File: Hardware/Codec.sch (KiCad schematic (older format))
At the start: 11 parts, among them U301 SGTL5000XNAA3

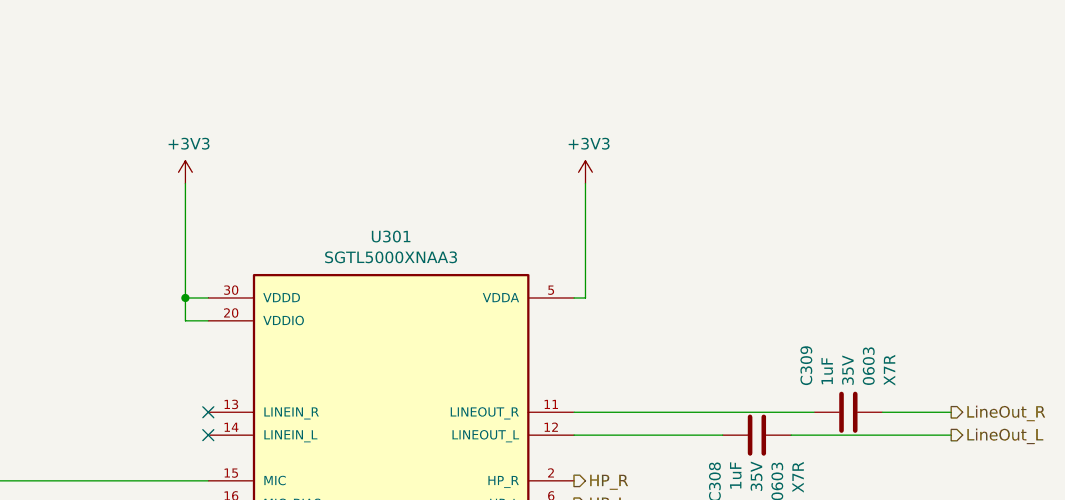
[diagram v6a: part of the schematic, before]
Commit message: Adding in extra decoupling.
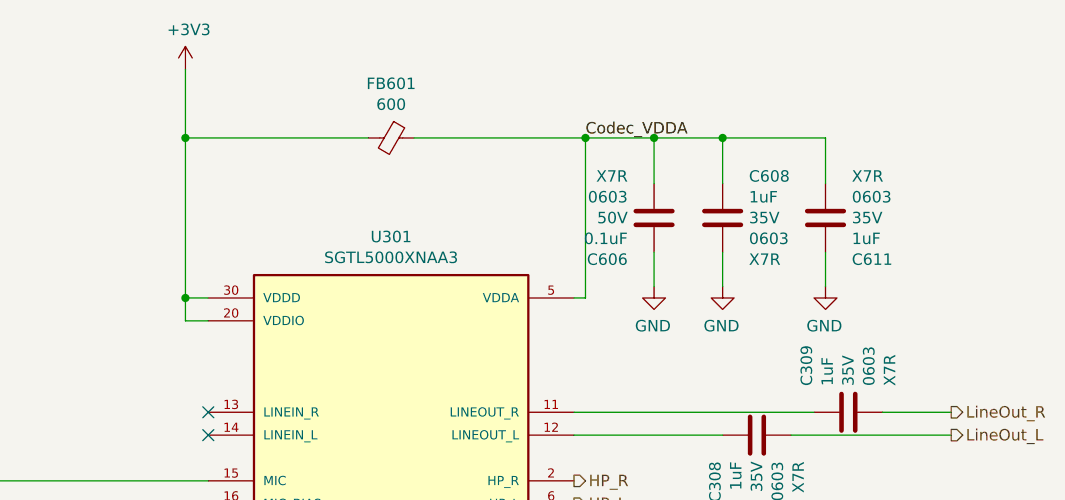
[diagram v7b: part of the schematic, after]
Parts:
- added C606: 0.1uF, Capacitor_SMD:C_0603_1608Metric, symbol Device:C
- added C608, C611: 1uF, Capacitor_SMD:C_0603_1608Metric, symbol Device:C
- added FB601: 600, Resistor_SMD:R_0603_1608Metric, symbol Device:Ferrite_Bead_Small
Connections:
- net +3V3: now also FB601.2; no longer U301.5 (VDDA)
- net GND: now also C606.1, C608.2, C611.1
- new net Codec_VDDA: C606.2, C608.1, C611.2, FB601.1, U301.5 (VDDA)
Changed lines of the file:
@@
 F 1 "SGTL5000XNAA3" H 5250 4726 50  0000 C CNN
 F 2 "Package_DFN_QFN:QFN-32-1EP_5x5mm_P0.5mm_EP3.65x3.65mm_ThermalVias" H 5250 3450 50  0001 L BNN
-F 3 "" H 5250 3450 50  0001 L BNN
+F 3 "https://www.nxp.com/docs/en/data-sheet/SGTL5000.pdf" H 5250 3450 50  0001 L BNN
 F 4 "Freescale Semiconductor" H 5250 3450 50  0001 L BNN "MANUFACTURER"
 F 5 "SGTL5000XNAA3" H 5250 3450 50  0001 C CNN "MPN"
@@
 L power:+3V3 #PWR?
 U 1 1 6145BB5A
-P 4350 1850
+P 4350 1350
 AR Path="/6123BB15/6145BB5A" Ref="#PWR?"  Part="1"
 AR Path="/611E335F/6145BB5A" Ref="#PWR?"  Part="1"
 AR Path="/611E3218/611E32E1/6145BB5A" Ref="#PWR0123"  Part="1"
-F 0 "#PWR0123" H 4350 1700 50  0001 C CNN
-F 1 "+3V3" H 4365 2023 50  0000 C CNN
-F 2 "" H 4350 1850 50  0001 C CNN
-F 3 "" H 4350 1850 50  0001 C CNN
-	1    4350 1850
+F 0 "#PWR0123" H 4350 1200 50  0001 C CNN
+F 1 "+3V3" H 4365 1523 50  0000 C CNN
+F 2 "" H 4350 1350 50  0001 C CNN
+F 3 "" H 4350 1350 50  0001 C CNN
+	1    4350 1350
 	1    0    0    -1
 $EndComp
@@
 	4450 2350 4350 2350
 Wire Wire Line
-	4350 2350 4350 1850
+	4350 2350 4350 1650
 Wire Wire Line
 	4450 2450 4350 2450
@@
 	-1   0    0    -1
 $EndComp
-$Comp
-L power:+3V3 #PWR?
-U 1 1 616AD8A4
-P 6100 1850
-AR Path="/6123BB15/616AD8A4" Ref="#PWR?"  Part="1"
-AR Path="/611E335F/616AD8A4" Ref="#PWR?"  Part="1"
-AR Path="/611E3218/611E32E1/616AD8A4" Ref="#PWR0181"  Part="1"
-F 0 "#PWR0181" H 6100 1700 50  0001 C CNN
-F 1 "+3V3" H 6115 2023 50  0000 C CNN
-F 2 "" H 6100 1850 50  0001 C CNN
-F 3 "" H 6100 1850 50  0001 C CNN
-	1    6100 1850
-	1    0    0    -1
-$EndComp
-Wire Wire Line
-	6100 1850 6100 2350
 Wire Wire Line
 	6100 2350 6050 2350
@@
 NoConn ~ 4450 2850
 NoConn ~ 4450 2950
+$Comp
+L Device:Ferrite_Bead_Small FB601
+U 1 1 61433A72
+P 5250 1650
+F 0 "FB601" V 5013 1650 50  0000 C CNN
+F 1 "600" V 5104 1650 50  0000 C CNN
+F 2 "Resistor_SMD:R_0603_1608Metric" V 5180 1650 50  0001 C CNN
+F 3 "~" H 5250 1650 50  0001 C CNN
+F 4 "BLM18AG601SN1D" V 5250 1650 50  0001 C CNN "MPN"
+F 5 "490-1014-1-ND" V 5250 1650 50  0001 C CNN "DPN"
+	1    5250 1650
+	0    1    1    0
+$EndComp
+Wire Wire Line
+	5350 1650 6100 1650
+Wire Wire Line
+	6100 1650 6100 2350
+Wire Wire Line
+	5150 1650 4350 1650
+Connection ~ 4350 1650
+Wire Wire Line
+	4350 1650 4350 1350
+Text Label 6100 1650 0    50   ~ 0
+Codec_VDDA
+$Comp
+L Device:C C?
+U 1 1 6143A1BC
+P 7150 2000
+AR Path="/611E335F/6143A1BC" Ref="C?"  Part="1"
+AR Path="/611E3218/611E32E1/6143A1BC" Ref="C611"  Part="1"
+AR Path="/611E3218/611E330D/6143A1BC" Ref="C?"  Part="1"
+F 0 "C611" H 7265 2182 50  0000 L CNN
+F 1 "1uF" H 7265 2091 50  0000 L CNN
+F 2 "Capacitor_SMD:C_0603_1608Metric" H 7188 1850 50  0001 C CNN
+F 3 "~" H 7150 2000 50  0001 C CNN
+F 4 "GMK107AB7105KAHT" H 7150 2000 50  0001 C CNN "MPN"
+F 5 "587-3352-1-ND" H 7150 2000 50  0001 C CNN "DPN"
+F 6 "35V" H 7265 2000 50  0000 L CNN "Tol"
+F 7 "0603" H 7265 1909 50  0000 L CNN "Pkg"
+F 8 "X7R" H 7265 1818 50  0000 L CNN "TCoff"
+	1    7150 2000
+	1    0    0    1
+$EndComp
+$Comp
+L Device:C C?
+U 1 1 6143AE76
+P 6700 2000
+AR Path="/611E335F/6143AE76" Ref="C?"  Part="1"
+AR Path="/611E3218/611E32E1/6143AE76" Ref="C608"  Part="1"
+F 0 "C608" H 6815 2182 50  0000 L CNN
+F 1 "1uF" H 6815 2091 50  0000 L CNN
+F 2 "Capacitor_SMD:C_0603_1608Metric" H 6738 1850 50  0001 C CNN
+F 3 "~" H 6700 2000 50  0001 C CNN
+F 4 "GMK107AB7105KAHT" H 6700 2000 50  0001 C CNN "MPN"
+F 5 "587-3352-1-ND" H 6700 2000 50  0001 C CNN "DPN"
+F 6 "35V" H 6815 2000 50  0000 L CNN "Tol"
+F 7 "0603" H 6815 1909 50  0000 L CNN "Pkg"
+F 8 "X7R" H 6815 1818 50  0000 L CNN "TCoff"
+	1    6700 2000
+	1    0    0    -1
+$EndComp
+$Comp
+L power:GND #PWR?
+U 1 1 6143B6DE
+P 6400 2300
+AR Path="/611E3335/6143B6DE" Ref="#PWR?"  Part="1"
+AR Path="/611E3218/611E32E1/6143B6DE" Ref="#PWR0181"  Part="1"
+F 0 "#PWR0181" H 6400 2050 50  0001 C CNN
+F 1 "GND" H 6405 2127 50  0000 C CNN
+F 2 "" H 6400 2300 50  0001 C CNN
+F 3 "" H 6400 2300 50  0001 C CNN
+	1    6400 2300
+	-1   0    0    -1
+$EndComp
+Wire Wire Line
+	6400 2150 6400 2300
+$Comp
+L power:GND #PWR?
+U 1 1 6143C88F
+P 6700 2300
+AR Path="/611E3335/6143C88F" Ref="#PWR?"  Part="1"
+AR Path="/611E3218/611E32E1/6143C88F" Ref="#PWR0184"  Part="1"
+F 0 "#PWR0184" H 6700 2050 50  0001 C CNN
+F 1 "GND" H 6705 2127 50  0000 C CNN
+F 2 "" H 6700 2300 50  0001 C CNN
+F 3 "" H 6700 2300 50  0001 C CNN
+	1    6700 2300
+	-1   0    0    -1
+$EndComp
+Wire Wire Line
+	6700 2150 6700 2300
+Wire Wire Line
+	6400 1850 6400 1650
+Wire Wire Line
+	6400 1650 6100 1650
+Connection ~ 6100 1650
+Wire Wire Line
+	6700 1650 6700 1850
+Wire Wire Line
+	6400 1650 6700 1650
+Connection ~ 6400 1650
+$Comp
+L Device:C C?
+U 1 1 61442973
+P 6400 2000
+AR Path="/611E335F/61442973" Ref="C?"  Part="1"
+AR Path="/611E3218/611E32E1/61442973" Ref="C606"  Part="1"
+F 0 "C606" H 6515 2182 50  0000 L CNN
+F 1 "0.1uF" H 6515 2091 50  0000 L CNN
+F 2 "Capacitor_SMD:C_0603_1608Metric" H 6438 1850 50  0001 C CNN
+F 3 "~" H 6400 2000 50  0001 C CNN
+F 4 "C0603C104K5RACAUTO" H 6400 2000 50  0001 C CNN "MPN"
+F 5 "399-6856-1-ND" H 6400 2000 50  0001 C CNN "DPN"
+F 6 "50V" H 6515 2000 50  0000 L CNN "Tol"
+F 7 "0603" H 6515 1909 50  0000 L CNN "Pkg"
+F 8 "X7R" H 6515 1818 50  0000 L CNN "TCoff"
+	1    6400 2000
+	-1   0    0    1
+$EndComp
+Wire Wire Line
+	6700 1650 7150 1650
+Wire Wire Line
+	7150 1650 7150 1850
+Connection ~ 6700 1650
+$Comp
+L power:GND #PWR?
+U 1 1 6144988F
+P 7150 2300
+AR Path="/611E3335/6144988F" Ref="#PWR?"  Part="1"
+AR Path="/611E3218/611E32E1/6144988F" Ref="#PWR0185"  Part="1"
+F 0 "#PWR0185" H 7150 2050 50  0001 C CNN
+F 1 "GND" H 7155 2127 50  0000 C CNN
+F 2 "" H 7150 2300 50  0001 C CNN
+F 3 "" H 7150 2300 50  0001 C CNN
+	1    7150 2300
+	-1   0    0    -1
+$EndComp
+Wire Wire Line
+	7150 2150 7150 2300
 $EndSCHEMATC

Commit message: Spare points on r=26.5mm @ x1.27mm linear separation.
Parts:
- removed C303: 1uF, Capacitor_SMD:C_0603_1608Metric, symbol Device:C
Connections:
- net +3V3: now also C302.1, C305.1
- net GND: now also C302.2, C305.2
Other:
- moved on the sheet: C302, C305
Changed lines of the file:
@@
 L Device:C C?
 U 1 1 6137DB9E
-P 2350 4850
+P 3400 1950
 AR Path="/611E335F/6137DB9E" Ref="C?"  Part="1"
 AR Path="/611E3218/611E32E1/6137DB9E" Ref="C302"  Part="1"
-F 0 "C302" H 2465 5032 50  0000 L CNN
-F 1 "1uF" H 2465 4941 50  0000 L CNN
-F 2 "Capacitor_SMD:C_0603_1608Metric" H 2388 4700 50  0001 C CNN
-F 3 "~" H 2350 4850 50  0001 C CNN
-F 4 "GMK107AB7105KAHT" H 2350 4850 50  0001 C CNN "MPN"
-F 5 "587-3352-1-ND" H 2350 4850 50  0001 C CNN "DPN"
-F 6 "35V" H 2465 4850 50  0000 L CNN "Tol"
-F 7 "0603" H 2465 4759 50  0000 L CNN "Pkg"
-F 8 "X7R" H 2465 4668 50  0000 L CNN "TCoff"
-	1    2350 4850
+F 0 "C302" H 3515 2132 50  0000 L CNN
+F 1 "1uF" H 3515 2041 50  0000 L CNN
+F 2 "Capacitor_SMD:C_0603_1608Metric" H 3438 1800 50  0001 C CNN
+F 3 "~" H 3400 1950 50  0001 C CNN
+F 4 "GMK107AB7105KAHT" H 3400 1950 50  0001 C CNN "MPN"
+F 5 "587-3352-1-ND" H 3400 1950 50  0001 C CNN "DPN"
+F 6 "35V" H 3515 1950 50  0000 L CNN "Tol"
+F 7 "0603" H 3515 1859 50  0000 L CNN "Pkg"
+F 8 "X7R" H 3515 1768 50  0000 L CNN "TCoff"
+	1    3400 1950
 	1    0    0    -1
 $EndComp
@@
 L Device:C C?
 U 1 1 6137E467
-P 2900 5600
+P 3900 1950
 AR Path="/611E335F/6137E467" Ref="C?"  Part="1"
 AR Path="/611E3218/611E32E1/6137E467" Ref="C305"  Part="1"
-F 0 "C305" H 3015 5782 50  0000 L CNN
-F 1 "0.1uF" H 3015 5691 50  0000 L CNN
-F 2 "Capacitor_SMD:C_0603_1608Metric" H 2938 5450 50  0001 C CNN
-F 3 "~" H 2900 5600 50  0001 C CNN
-F 4 "C0603C104K5RACAUTO" H 2900 5600 50  0001 C CNN "MPN"
-F 5 "399-6856-1-ND" H 2900 5600 50  0001 C CNN "DPN"
-F 6 "50V" H 3015 5600 50  0000 L CNN "Tol"
-F 7 "0603" H 3015 5509 50  0000 L CNN "Pkg"
-F 8 "X7R" H 3015 5418 50  0000 L CNN "TCoff"
-	1    2900 5600
-	1    0    0    -1
-$EndComp
-$Comp
-L Device:C C?
-U 1 1 6137E472
-P 2350 5600
-AR Path="/611E335F/6137E472" Ref="C?"  Part="1"
-AR Path="/611E3218/611E32E1/6137E472" Ref="C303"  Part="1"
-F 0 "C303" H 2465 5782 50  0000 L CNN
-F 1 "1uF" H 2465 5691 50  0000 L CNN
-F 2 "Capacitor_SMD:C_0603_1608Metric" H 2388 5450 50  0001 C CNN
-F 3 "~" H 2350 5600 50  0001 C CNN
-F 4 "GMK107AB7105KAHT" H 2350 5600 50  0001 C CNN "MPN"
-F 5 "587-3352-1-ND" H 2350 5600 50  0001 C CNN "DPN"
-F 6 "35V" H 2465 5600 50  0000 L CNN "Tol"
-F 7 "0603" H 2465 5509 50  0000 L CNN "Pkg"
-F 8 "X7R" H 2465 5418 50  0000 L CNN "TCoff"
-	1    2350 5600
+F 0 "C305" H 4015 2132 50  0000 L CNN
+F 1 "0.1uF" H 4015 2041 50  0000 L CNN
+F 2 "Capacitor_SMD:C_0603_1608Metric" H 3938 1800 50  0001 C CNN
+F 3 "~" H 3900 1950 50  0001 C CNN
+F 4 "C0603C104K5RACAUTO" H 3900 1950 50  0001 C CNN "MPN"
+F 5 "399-6856-1-ND" H 3900 1950 50  0001 C CNN "DPN"
+F 6 "50V" H 4015 1950 50  0000 L CNN "Tol"
+F 7 "0603" H 4015 1859 50  0000 L CNN "Pkg"
+F 8 "X7R" H 4015 1768 50  0000 L CNN "TCoff"
+	1    3900 1950
 	1    0    0    -1
 $EndComp
@@
 Wire Wire Line
 	7150 2150 7150 2300
+Wire Wire Line
+	4350 1650 3900 1650
+Wire Wire Line
+	3900 1650 3900 1800
+$Comp
+L power:GND #PWR?
+U 1 1 616E0107
+P 3900 2550
+AR Path="/611E3335/616E0107" Ref="#PWR?"  Part="1"
+AR Path="/611E3218/611E32E1/616E0107" Ref="#PWR0193"  Part="1"
+F 0 "#PWR0193" H 3900 2300 50  0001 C CNN
+F 1 "GND" H 3905 2377 50  0000 C CNN
+F 2 "" H 3900 2550 50  0001 C CNN
+F 3 "" H 3900 2550 50  0001 C CNN
+	1    3900 2550
+	-1   0    0    -1
+$EndComp
+Wire Wire Line
+	3900 2100 3900 2550
+Wire Wire Line
+	3900 1650 3400 1650
+Wire Wire Line
+	3400 1650 3400 1800
+Connection ~ 3900 1650
+$Comp
+L power:GND #PWR?
+U 1 1 616F15CC
+P 3400 2550
+AR Path="/611E3335/616F15CC" Ref="#PWR?"  Part="1"
+AR Path="/611E3218/611E32E1/616F15CC" Ref="#PWR0194"  Part="1"
+F 0 "#PWR0194" H 3400 2300 50  0001 C CNN
+F 1 "GND" H 3405 2377 50  0000 C CNN
+F 2 "" H 3400 2550 50  0001 C CNN
+F 3 "" H 3400 2550 50  0001 C CNN
+	1    3400 2550
+	-1   0    0    -1
+$EndComp
+Wire Wire Line
+	3400 2100 3400 2550
 $EndSCHEMATC
